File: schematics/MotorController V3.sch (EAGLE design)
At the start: 53 parts, among them IC1 7805, Q1 BC307

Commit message: no message
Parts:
- R1, R10, R12, R13, R14, R15, R2, R3, R4, R5, R6, R7, R8, R9: device resistor:R-EU_0204/7 -> rcl:R-EU_0207/10
- U$3: value NODEMCU -> NODEMCUNODEMCUV2; device nodemcu:NODEMCU -> nodemcu:NODEMCUNODEMCUV2
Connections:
- net SCL1: now also U$3.D2; no longer U$3.D1
- net SDA1: now also U$3.D1; no longer U$3.D2
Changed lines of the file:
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@@
 <part name="P+1" library="supply1" library_urn="urn:adsk.eagle:library:371" deviceset="VCC" device=""/>
 <part name="GND1" library="supply1" library_urn="urn:adsk.eagle:library:371" deviceset="GND" device=""/>
-<part name="R1" library="resistor" library_urn="urn:adsk.eagle:library:348" deviceset="R-EU_" device="0204/7" package3d_urn="urn:adsk.eagle:package:25945/1" value="1K"/>
-<part name="R2" library="resistor" library_urn="urn:adsk.eagle:library:348" deviceset="R-EU_" device="0204/7" package3d_urn="urn:adsk.eagle:package:25945/1" value="1K"/>
-<part name="R3" library="resistor" library_urn="urn:adsk.eagle:library:348" deviceset="R-EU_" device="0204/7" package3d_urn="urn:adsk.eagle:package:25945/1" value="1K"/>
+<part name="R1" library="rcl" library_urn="urn:adsk.eagle:library:334" deviceset="R-EU_" device="0207/10" package3d_urn="urn:adsk.eagle:package:23491/1" value="1K"/>
+<part name="R2" library="rcl" library_urn="urn:adsk.eagle:library:334" deviceset="R-EU_" device="0207/10" package3d_urn="urn:adsk.eagle:package:23491/1" value="1K"/>
+<part name="R3" library="rcl" library_urn="urn:adsk.eagle:library:334" deviceset="R-EU_" device="0207/10" package3d_urn="urn:adsk.eagle:package:23491/1" value="1K"/>
 <part name="DRK2" library="Drotek L6234" deviceset="DROTEKL6234" device=""/>
 <part name="DRK3" library="Drotek L6234" deviceset="DROTEKL6234" device=""/>
-<part name="R4" library="resistor" library_urn="urn:adsk.eagle:library:348" deviceset="R-EU_" device="0204/7" package3d_urn="urn:adsk.eagle:package:25945/1" value="330"/>
-<part name="R5" library="resistor" library_urn="urn:adsk.eagle:library:348" deviceset="R-EU_" device="0204/7" package3d_urn="urn:adsk.eagle:package:25945/1" value="330"/>
-<part name="R6" library="resistor" library_urn="urn:adsk.eagle:library:348" deviceset="R-EU_" device="0204/7" package3d_urn="urn:adsk.eagle:package:25945/1" value="330"/>
-<part name="R7" library="resistor" library_urn="urn:adsk.eagle:library:348" deviceset="R-EU_" device="0204/7" package3d_urn="urn:adsk.eagle:package:25945/1" value="330"/>
-<part name="R8" library="resistor" library_urn="urn:adsk.eagle:library:348" deviceset="R-EU_" device="0204/7" package3d_urn="urn:adsk.eagle:package:25945/1" value="330"/>
-<part name="R9" library="resistor" library_urn="urn:adsk.eagle:library:348" deviceset="R-EU_" device="0204/7" package3d_urn="urn:adsk.eagle:package:25945/1" value="330"/>
-<part name="R10" library="resistor" library_urn="urn:adsk.eagle:library:348" deviceset="R-EU_" device="0204/7" package3d_urn="urn:adsk.eagle:package:25945/1" value="1K"/>
+<part name="R4" library="rcl" library_urn="urn:adsk.eagle:library:334" deviceset="R-EU_" device="0207/10" package3d_urn="urn:adsk.eagle:package:23491/1" value="330"/>
+<part name="R5" library="rcl" library_urn="urn:adsk.eagle:library:334" deviceset="R-EU_" device="0207/10" package3d_urn="urn:adsk.eagle:package:23491/1" value="330"/>
+<part name="R6" library="rcl" library_urn="urn:adsk.eagle:library:334" deviceset="R-EU_" device="0207/10" package3d_urn="urn:adsk.eagle:package:23491/1" value="330"/>
+<part name="R7" library="rcl" library_urn="urn:adsk.eagle:library:334" deviceset="R-EU_" device="0207/10" package3d_urn="urn:adsk.eagle:package:23491/1" value="330"/>
+<part name="R8" library="rcl" library_urn="urn:adsk.eagle:library:334" deviceset="R-EU_" device="0207/10" package3d_urn="urn:adsk.eagle:package:23491/1" value="330"/>
+<part name="R9" library="rcl" library_urn="urn:adsk.eagle:library:334" deviceset="R-EU_" device="0207/10" package3d_urn="urn:adsk.eagle:package:23491/1" value="330"/>
+<part name="R10" library="rcl" library_urn="urn:adsk.eagle:library:334" deviceset="R-EU_" device="0207/10" package3d_urn="urn:adsk.eagle:package:23491/1" value="1K"/>
 <part name="ENCODER3" library="con-lstb" library_urn="urn:adsk.eagle:library:162" deviceset="MA04-1" device="" package3d_urn="urn:adsk.eagle:package:8337/1" value="1"/>
 <part name="ENCODER1" library="con-lstb" library_urn="urn:adsk.eagle:library:162" deviceset="MA04-1" device="" package3d_urn="urn:adsk.eagle:package:8337/1" value="1"/>
@@
 <part name="CONTROL" library="con-lstb" library_urn="urn:adsk.eagle:library:162" deviceset="MA08-1" device="" package3d_urn="urn:adsk.eagle:package:8343/1" value=" "/>
 <part name="D3" library="diode" library_urn="urn:adsk.eagle:library:210" deviceset="1N581*" device="" package3d_urn="urn:adsk.eagle:package:43421/1" technology="8-B"/>
-<part name="R12" library="resistor" library_urn="urn:adsk.eagle:library:348" deviceset="R-EU_" device="0204/7" package3d_urn="urn:adsk.eagle:package:25945/1" value="1K"/>
+<part name="R12" library="rcl" library_urn="urn:adsk.eagle:library:334" deviceset="R-EU_" device="0207/10" package3d_urn="urn:adsk.eagle:package:23491/1" value="1K"/>
 <part name="D4" library="diode" library_urn="urn:adsk.eagle:library:210" deviceset="ZENER-DIODE" device="DO41Z10" package3d_urn="urn:adsk.eagle:package:43341/1" value="5.6V"/>
 <part name="D5" library="diode" library_urn="urn:adsk.eagle:library:210" deviceset="ZENER-DIODE" device="DO41Z10" package3d_urn="urn:adsk.eagle:package:43341/1" value="5.6V"/>
 <part name="D6" library="diode" library_urn="urn:adsk.eagle:library:210" deviceset="ZENER-DIODE" device="DO41Z10" package3d_urn="urn:adsk.eagle:package:43341/1" value="5.6V"/>
 <part name="D7" library="diode" library_urn="urn:adsk.eagle:library:210" deviceset="ZENER-DIODE" device="DO41Z10" package3d_urn="urn:adsk.eagle:package:43341/1" value="5.6V"/>
-<part name="R13" library="resistor" library_urn="urn:adsk.eagle:library:348" deviceset="R-EU_" device="0204/7" package3d_urn="urn:adsk.eagle:package:25945/1" value="1K"/>
-<part name="R14" library="resistor" library_urn="urn:adsk.eagle:library:348" deviceset="R-EU_" device="0204/7" package3d_urn="urn:adsk.eagle:package:25945/1" value="1K"/>
+<part name="R13" library="rcl" library_urn="urn:adsk.eagle:library:334" deviceset="R-EU_" device="0207/10" package3d_urn="urn:adsk.eagle:package:23491/1" value="1K"/>
+<part name="R14" library="rcl" library_urn="urn:adsk.eagle:library:334" deviceset="R-EU_" device="0207/10" package3d_urn="urn:adsk.eagle:package:23491/1" value="1K"/>
 <part name="D8" library="diode" library_urn="urn:adsk.eagle:library:210" deviceset="ZENER-DIODE" device="DO41Z10" package3d_urn="urn:adsk.eagle:package:43341/1" value="5.6V"/>
 <part name="D9" library="diode" library_urn="urn:adsk.eagle:library:210" deviceset="ZENER-DIODE" device="DO41Z10" package3d_urn="urn:adsk.eagle:package:43341/1" value="5.6V"/>
@@
 <part name="D12" library="diode" library_urn="urn:adsk.eagle:library:210" deviceset="ZENER-DIODE" device="DO41Z10" package3d_urn="urn:adsk.eagle:package:43341/1" value="5.6V"/>
 <part name="D13" library="diode" library_urn="urn:adsk.eagle:library:210" deviceset="ZENER-DIODE" device="DO41Z10" package3d_urn="urn:adsk.eagle:package:43341/1" value="5.6V"/>
-<part name="U$3" library="nodemcu" deviceset="NODEMCU" device=""/>
+<part name="U$3" library="nodemcu" deviceset="NODEMCU" device="NODEMCUV2" value="NODEMCUNODEMCUV2"/>
 <part name="LED1" library="led" library_urn="urn:adsk.eagle:library:259" deviceset="LED" device="3MM" package3d_urn="urn:adsk.eagle:package:15797/1" value="red"/>
-<part name="R15" library="resistor" library_urn="urn:adsk.eagle:library:348" deviceset="R-EU_" device="0204/7" package3d_urn="urn:adsk.eagle:package:25945/1" value="4,7K"/>
+<part name="R15" library="rcl" library_urn="urn:adsk.eagle:library:334" deviceset="R-EU_" device="0207/10" package3d_urn="urn:adsk.eagle:package:23491/1" value="4,7K"/>
 <part name="MOTOR1" library="con-molex" deviceset="5566-4" device=""/>
 <part name="MOTOR2" library="con-molex" deviceset="5566-4" device=""/>
@@
 <instance part="Q1" gate="G$1" x="-58.42" y="7.62">
 <attribute name="NAME" x="-68.58" y="15.24" size="1.778" layer="95"/>
-<attribute name="VALUE" x="-55.88" y="7.62" size="1.778" layer="96"/>
+<attribute name="VALUE" x="-68.58" y="12.7" size="1.778" layer="96"/>
 </instance>
 <instance part="R11" gate="G$1" x="-121.92" y="-30.48" rot="R90">
@@
 <wire x1="73.66" y1="154.94" x2="73.66" y2="114.3" width="0.1524" layer="91"/>
 <label x="73.66" y="114.3" size="1.778" layer="95" rot="R90"/>
-<wire x1="73.66" y1="154.94" x2="71.12" y2="154.94" width="0.1524" layer="91"/>
-<pinref part="U$3" gate="G$1" pin="D1"/>
-<wire x1="73.66" y1="190.5" x2="71.12" y2="190.5" width="0.1524" layer="91"/>
-<wire x1="71.12" y1="190.5" x2="71.12" y2="154.94" width="0.1524" layer="91"/>
-</segment>
-</net>
-<net name="SDA1" class="0">
-<segment>
-<pinref part="PRJ1" gate="G$1" pin="37/A18"/>
-<wire x1="76.2" y1="162.56" x2="76.2" y2="114.3" width="0.1524" layer="91"/>
-<label x="76.2" y="114.3" size="1.778" layer="95" rot="R90"/>
 <pinref part="U$3" gate="G$1" pin="D2"/>
 <wire x1="68.58" y1="193.04" x2="73.66" y2="193.04" width="0.1524" layer="91"/>
-<wire x1="68.58" y1="193.04" x2="68.58" y2="162.56" width="0.1524" layer="91"/>
-<wire x1="68.58" y1="162.56" x2="76.2" y2="162.56" width="0.1524" layer="91"/>
-</segment>
-</net>
+<wire x1="68.58" y1="193.04" x2="68.58" y2="154.94" width="0.1524" layer="91"/>
+<wire x1="68.58" y1="154.94" x2="73.66" y2="154.94" width="0.1524" layer="91"/>
+</segment>
+</net>
+<net name="SDA1" class="0">
+<segment>
+<pinref part="PRJ1" gate="G$1" pin="37/A18"/>
+<label x="76.2" y="114.3" size="1.778" layer="95" rot="R90"/>
+<pinref part="U$3" gate="G$1" pin="D1"/>
+<wire x1="76.2" y1="157.48" x2="76.2" y2="114.3" width="0.1524" layer="91"/>
+<wire x1="73.66" y1="190.5" x2="71.12" y2="190.5" width="0.1524" layer="91"/>
+<wire x1="71.12" y1="190.5" x2="71.12" y2="157.48" width="0.1524" layer="91"/>
+<wire x1="71.12" y1="157.48" x2="76.2" y2="157.48" width="0.1524" layer="91"/>
+</segment>
+</net>

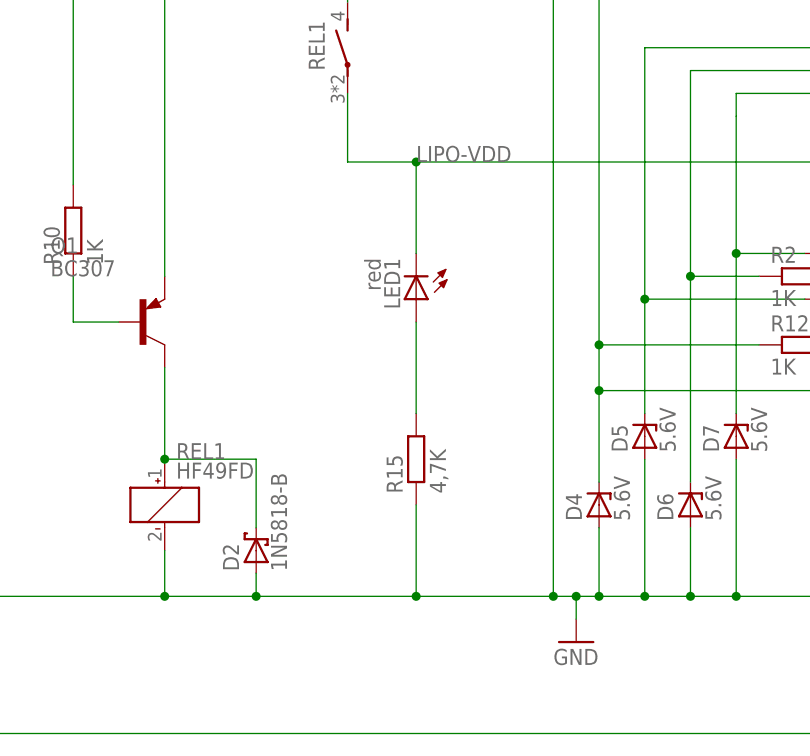
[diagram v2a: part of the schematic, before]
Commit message: calibrated PID of lifter motor
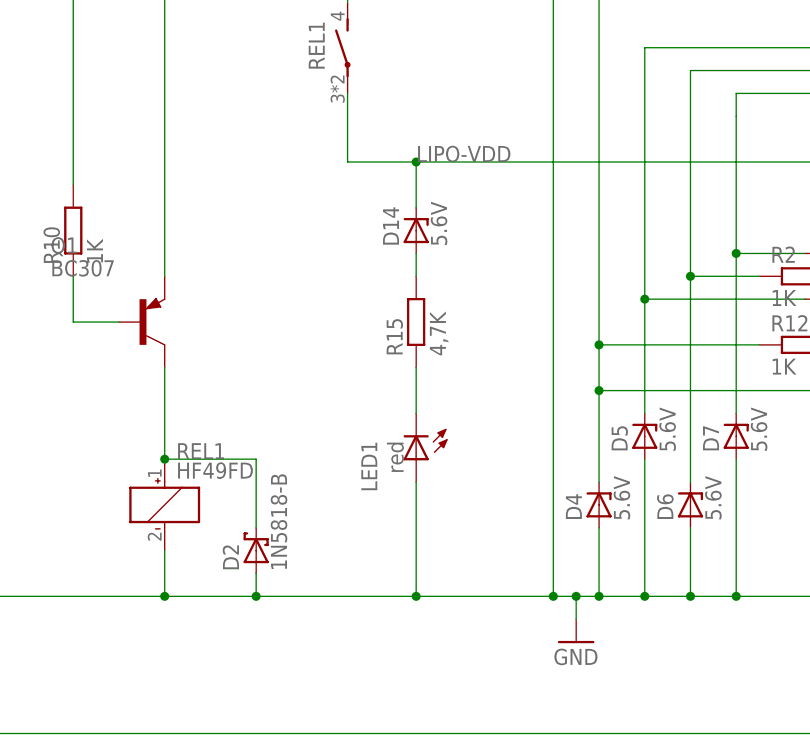
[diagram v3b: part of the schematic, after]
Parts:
- added D14: 5.6V, diode:ZENER-DIODEDO41Z10
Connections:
- removed net N$41: LED1.A, R15.2
- new net N$33: D14.A, R15.2
- new net N$34: LED1.C, R15.1
- net GND: now also LED1.A; no longer R15.1
- net LIPO-VDD: now also D14.C; no longer LED1.C
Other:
- moved on the sheet: LED1, R15
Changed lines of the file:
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@@
 <part name="MOTOR2" library="con-molex" deviceset="5566-4" device=""/>
 <part name="MOTOR3" library="con-molex" deviceset="5566-4" device=""/>
+<part name="D14" library="diode" library_urn="urn:adsk.eagle:library:210" deviceset="ZENER-DIODE" device="DO41Z10" package3d_urn="urn:adsk.eagle:package:43341/1" value="5.6V"/>
 </parts>
 <sheets>
@@
 </instance>
 <instance part="U$3" gate="G$1" x="93.98" y="205.74" rot="R180"/>
-<instance part="LED1" gate="G$1" x="-27.94" y="10.16" rot="R180">
-<attribute name="NAME" x="-31.496" y="14.732" size="1.778" layer="95" rot="R270"/>
-<attribute name="VALUE" x="-33.655" y="14.732" size="1.778" layer="96" rot="R270"/>
-</instance>
-<instance part="R15" gate="G$1" x="-27.94" y="-7.62" rot="R90">
-<attribute name="NAME" x="-29.4386" y="-11.43" size="1.778" layer="95" rot="R90"/>
-<attribute name="VALUE" x="-24.638" y="-11.43" size="1.778" layer="96" rot="R90"/>
+<instance part="LED1" gate="G$1" x="-27.94" y="-7.62" rot="R180">
+<attribute name="NAME" x="-34.036" y="-5.588" size="1.778" layer="95" rot="R270"/>
+<attribute name="VALUE" x="-31.115" y="-5.588" size="1.778" layer="96" rot="R270"/>
+</instance>
+<instance part="R15" gate="G$1" x="-27.94" y="7.62" rot="R90">
+<attribute name="NAME" x="-29.4386" y="3.81" size="1.778" layer="95" rot="R90"/>
+<attribute name="VALUE" x="-24.638" y="3.81" size="1.778" layer="96" rot="R90"/>
 </instance>
 <instance part="MOTOR1" gate="-1" x="48.26" y="-12.7" rot="R270">
@@
 <instance part="MOTOR3" gate="-4" x="170.18" y="-12.7" rot="R270">
 <attribute name="NAME" x="169.418" y="-15.24" size="1.524" layer="95" rot="R270"/>
+</instance>
+<instance part="D14" gate="G$1" x="-27.94" y="17.78" rot="R90">
+<attribute name="NAME" x="-29.845" y="16.002" size="1.778" layer="95" rot="R90"/>
+<attribute name="VALUE" x="-24.511" y="16.002" size="1.778" layer="96" rot="R90"/>
 </instance>
 </instances>
@@
 <junction x="137.16" y="124.46"/>
 <label x="134.62" y="162.56" size="1.778" layer="95"/>
-<pinref part="R15" gate="G$1" pin="1"/>
-<wire x1="-27.94" y1="-12.7" x2="-27.94" y2="-22.86" width="0.1524" layer="91"/>
-<junction x="-27.94" y="-22.86"/>
 <pinref part="U$3" gate="G$1" pin="GND"/>
 <wire x1="114.3" y1="190.5" x2="116.84" y2="190.5" width="0.1524" layer="91"/>
@@
 <label x="177.8" y="68.58" size="1.778" layer="95"/>
 <label x="177.8" y="86.36" size="1.778" layer="95"/>
+<pinref part="LED1" gate="G$1" pin="A"/>
+<wire x1="-27.94" y1="-10.16" x2="-27.94" y2="-22.86" width="0.1524" layer="91"/>
+<junction x="-27.94" y="-22.86"/>
 </segment>
 </net>
@@
 <net name="LIPO-VDD" class="1">
 <segment>
+<pinref part="DRK1" gate="G$1" pin="LIPO+"/>
 <wire x1="-35.56" y1="25.4" x2="-27.94" y2="25.4" width="0.1524" layer="91"/>
-<pinref part="DRK1" gate="G$1" pin="LIPO+"/>
 <wire x1="-27.94" y1="25.4" x2="55.88" y2="25.4" width="0.1524" layer="91"/>
 <wire x1="55.88" y1="25.4" x2="55.88" y2="15.24" width="0.1524" layer="91"/>
@@
 <pinref part="U$1" gate="G$1" pin="VIN(5-28V)"/>
 <pinref part="REL1" gate="G$1" pin="P"/>
-<pinref part="LED1" gate="G$1" pin="C"/>
-<wire x1="-27.94" y1="15.24" x2="-27.94" y2="25.4" width="0.1524" layer="91"/>
+<pinref part="D14" gate="G$1" pin="C"/>
+<wire x1="-27.94" y1="20.32" x2="-27.94" y2="25.4" width="0.1524" layer="91"/>
 <junction x="-27.94" y="25.4"/>
 </segment>
@@
 </segment>
 </net>
-<net name="N$41" class="0">
-<segment>
-<pinref part="R15" gate="G$1" pin="2"/>
-<pinref part="LED1" gate="G$1" pin="A"/>
-<wire x1="-27.94" y1="-2.54" x2="-27.94" y2="7.62" width="0.1524" layer="91"/>
-</segment>
-</net>
 <net name="RST" class="0">
 <segment>
@@
 </segment>
 </net>
+<net name="N$33" class="0">
+<segment>
+<pinref part="D14" gate="G$1" pin="A"/>
+<pinref part="R15" gate="G$1" pin="2"/>
+<wire x1="-27.94" y1="15.24" x2="-27.94" y2="12.7" width="0.1524" layer="91"/>
+</segment>
+</net>
+<net name="N$34" class="0">
+<segment>
+<pinref part="R15" gate="G$1" pin="1"/>
+<pinref part="LED1" gate="G$1" pin="C"/>
+<wire x1="-27.94" y1="2.54" x2="-27.94" y2="-2.54" width="0.1524" layer="91"/>
+</segment>
+</net>
